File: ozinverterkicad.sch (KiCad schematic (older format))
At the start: 65 parts, among them P1 CONN_02X05, P2 CONN_01X02, P3 on/off, P4 temp, P5 ct sense, P6 Active mains, P7 neutral mains, P8 systemled, Q2 tip35c, T1 12vac transforme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

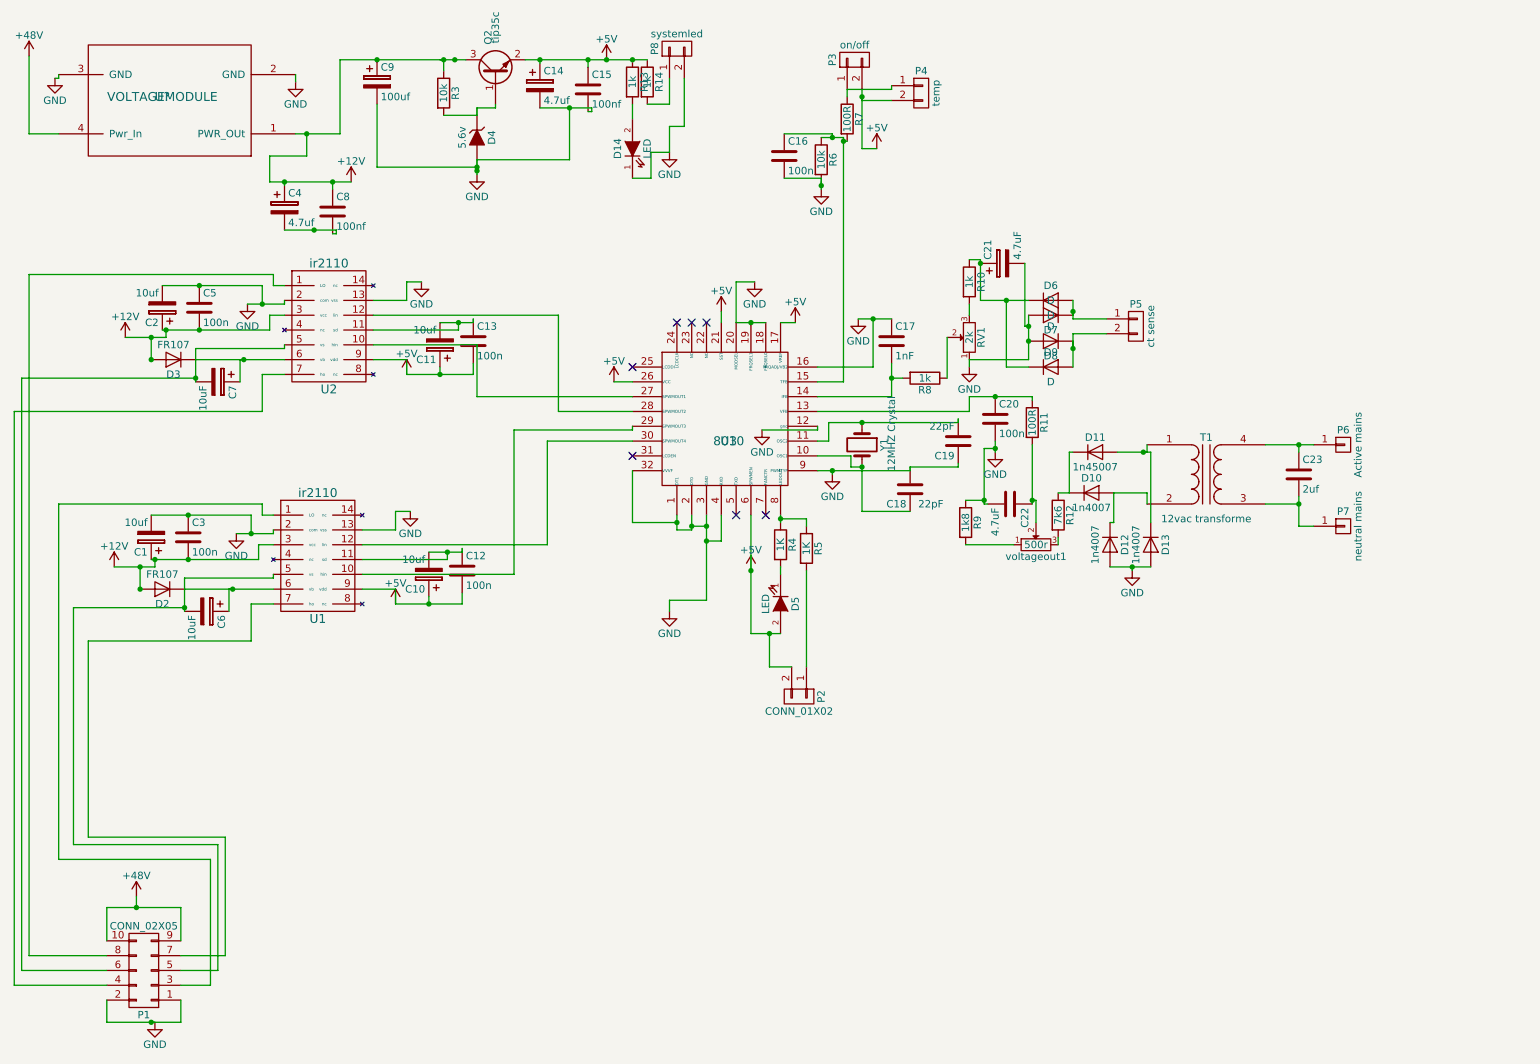
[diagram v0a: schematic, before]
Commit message: added extra ct sense
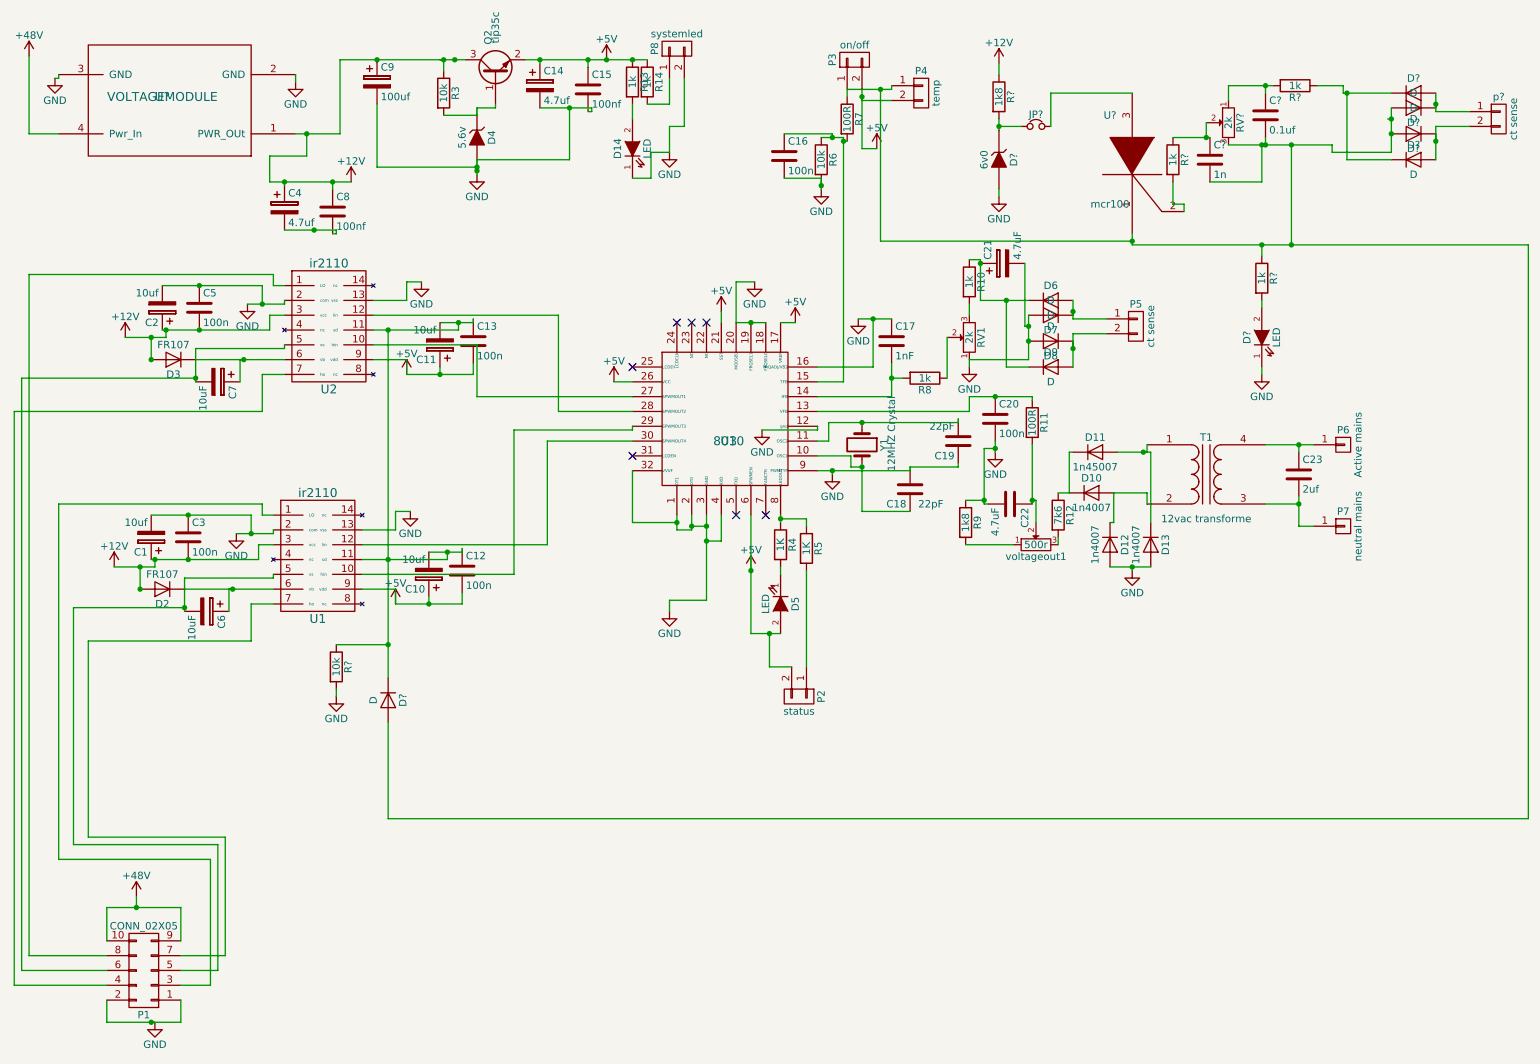
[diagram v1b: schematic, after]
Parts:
- added C?: 1n, symbol C
- added C?: 0.1uf, symbol C
- added D?: 6v0, symbol ZENER
- added D? (x4): D, Diodes_ThroughHole:Diode_DO-41_SOD81_Vertical_AnodeUp, symbol D
- added D?: LED, symbol LED
- added D?: D, symbol D
- added JP?: reset, symbol Jumper_NC_Small
- added R?: 1k8, symbol R
- added R? (x3): 1k, symbol R
- added R?: 10k, symbol R
- added RV?: 2k, Discret:RV2X4, symbol POT
- added U?: mcr100, symbol SCR
- added p?: ct sense, Connectors_Molex:Molex_KK-6410-02_02x2.54mm_Straight, symbol CONN_01X02
- P2: value CONN_01X02 -> status
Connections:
- net +12V: now also R?.1
- net GND: now also D?.1 (K), D?.2 (A), R?.2
- net at P3.1 (P1), P4.1 (P1), R7.1: now also C?.2, C?.2, D?.2 (A), D?.2 (A), D?.2 (A), R?.1, RV?.3, U?.1 (K)
- net at C11.2, C13.1, U2.11 (sd): now also C10.2, C12.1, U1.11 (sd), D?.1 (K), R?.1
- new net: D?.1 (K), JP?.1, R?.2
- new net: JP?.2, U?.3 (A)
- new net: D?.1 (K), D?.1 (K), R?.1
- new net: D?.1 (K), D?.2 (A), p?.1 (P1)
- new net: D?.1 (K), D?.2 (A), p?.2 (P2)
- new net: C?.1, R?.2, RV?.1
- new net: C?.1, R?.1, RV?.2
- new net: R?.2, U?.2 (G)
- new net: D?.2 (A), R?.2

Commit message: added extra ct routed
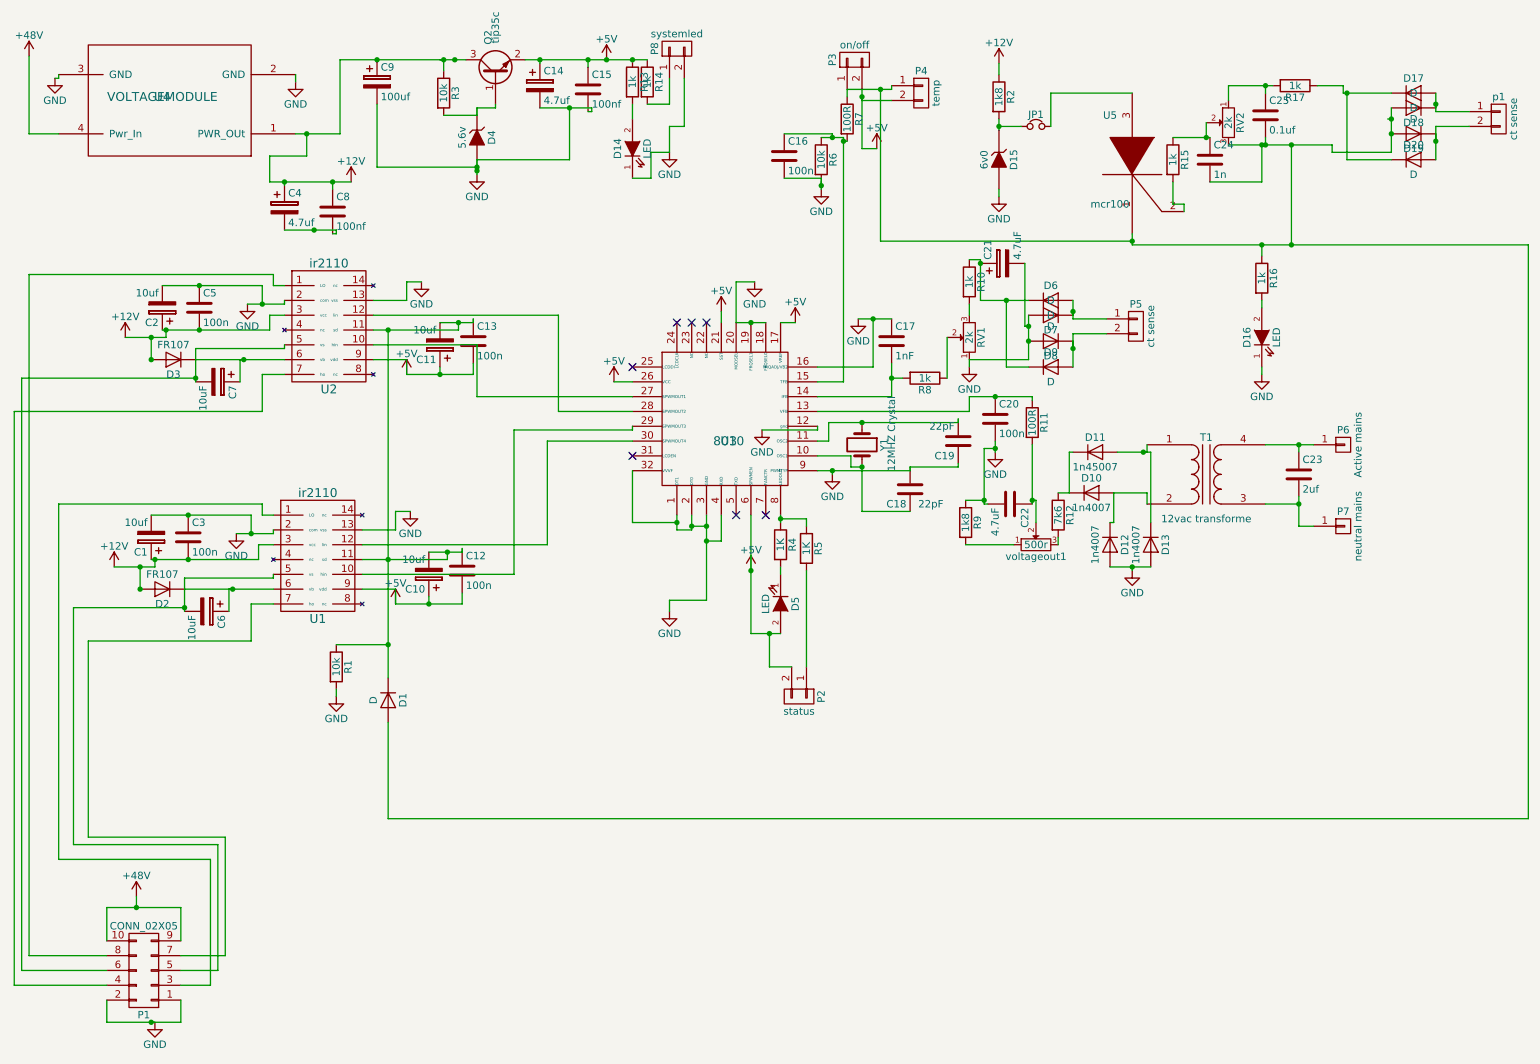
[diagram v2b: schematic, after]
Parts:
- C24: renamed from C?; footprint (none) -> Capacitors_ThroughHole:C_Disc_D3_P2.5
- C25: renamed from C?; footprint (none) -> Capacitors_ThroughHole:C_Radial_D5_L6_P2.5
- D1, D15: renamed from D?; footprint (none) -> Diodes_ThroughHole:Diode_DO-41_SOD81_Vertical_AnodeUp
- D16: renamed from D?; footprint (none) -> LEDs:LED-5MM
- JP1: renamed from JP?; footprint (none) -> Connectors_Molex:Molex_KK-6410-02_02x2.54mm_Straight
- R1, R15, R16, R17, R2: renamed from R?; footprint (none) -> Resistors_ThroughHole:Resistor_Horizontal_RM7mm
- U4: renamed from U?; footprint (none) -> ozinverterkicad:lm2596hvsmodule
- U5: renamed from U?; footprint (none) -> TO_SOT_Packages_THT:TO-92_Molded_Narrow
- gave numbers to parts that had none: 6
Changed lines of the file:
@@
 $EndComp
 $Comp
-L +12V #PWR027
+L +12V #PWR026
 U 1 1 57CBBFC9
 P 2825 1725
-F 0 "#PWR027" H 2825 1575 50  0001 C CNN
+F 0 "#PWR026" H 2825 1575 50  0001 C CNN
 F 1 "+12V" H 2825 1865 50  0000 C CNN
 F 2 "" H 2825 1725 50  0000 C CNN
@@
 $EndComp
 $Comp
-L GND #PWR028
+L GND #PWR027
 U 1 1 57CBD12F
 P 3675 1675
-F 0 "#PWR028" H 3675 1425 50  0001 C CNN
+F 0 "#PWR027" H 3675 1425 50  0001 C CNN
 F 1 "GND" H 3675 1525 50  0000 C CNN
 F 2 "" H 3675 1675 50  0000 C CNN
@@
 $EndComp
 $Comp
-L +5V #PWR029
+L +5V #PWR028
 U 1 1 57CBD147
 P 4550 900
-F 0 "#PWR029" H 4550 750 50  0001 C CNN
+F 0 "#PWR028" H 4550 750 50  0001 C CNN
 F 1 "+5V" H 4550 1040 50  0000 C CNN
 F 2 "" H 4550 900 50  0000 C CNN
@@
 $EndComp
 $Comp
-L GND #PWR030
+L GND #PWR029
 U 1 1 57CC63F3
 P 4975 1525
-F 0 "#PWR030" H 4975 1275 50  0001 C CNN
+F 0 "#PWR029" H 4975 1275 50  0001 C CNN
 F 1 "GND" H 4975 1375 50  0000 C CNN
 F 2 "" H 4975 1525 50  0000 C CNN
@@
 $EndComp
 $Comp
-L VOLTAGEMODULE U?
+L VOLTAGEMODULE U4
 U 1 1 57CBBBB1
 P 1550 1150
-F 0 "U?" H 1550 1150 60  0000 C CNN
+F 0 "U4" H 1550 1150 60  0000 C CNN
 F 1 "VOLTAGEMODULE" H 1550 1150 60  0000 C CNN
-F 2 "" H 1550 1150 60  0000 C CNN
+F 2 "ozinverterkicad:lm2596hvsmodule" H 1550 1150 60  0001 C CNN
 F 3 "" H 1550 1150 60  0000 C CNN
 	1    1550 1150
@@
 $EndComp
 $Comp
-L GND #PWR?
+L GND #PWR030
 U 1 1 57CBDA8B
 P 825 1025
-F 0 "#PWR?" H 825 775 50  0001 C CNN
+F 0 "#PWR030" H 825 775 50  0001 C CNN
 F 1 "GND" H 825 875 50  0000 C CNN
 F 2 "" H 825 1025 50  0000 C CNN
@@
 $EndComp
 $Comp
-L GND #PWR?
+L GND #PWR031
 U 1 1 57CBE302
 P 2450 1050
-F 0 "#PWR?" H 2450 800 50  0001 C CNN
+F 0 "#PWR031" H 2450 800 50  0001 C CNN
 F 1 "GND" H 2450 900 50  0000 C CNN
 F 2 "" H 2450 1050 50  0000 C CNN
@@
 $EndComp
 $Comp
-L ZENER D?
+L ZENER D15
 U 1 1 58022F88
 P 7200 1575
-F 0 "D?" H 7200 1675 50  0000 C CNN
+F 0 "D15" H 7200 1675 50  0000 C CNN
 F 1 "6v0" H 7200 1475 50  0000 C CNN
-F 2 "" H 7200 1575 50  0000 C CNN
+F 2 "Diodes_ThroughHole:Diode_DO-41_SOD81_Vertical_AnodeUp" H 7200 1575 50  0001 C CNN
 F 3 "" H 7200 1575 50  0000 C CNN
 	1    7200 1575
@@
 $EndComp
 $Comp
-L GND #PWR?
+L GND #PWR032
 U 1 1 580231C8
 P 7200 1825
-F 0 "#PWR?" H 7200 1575 50  0001 C CNN
+F 0 "#PWR032" H 7200 1575 50  0001 C CNN
 F 1 "GND" H 7200 1675 50  0000 C CNN
 F 2 "" H 7200 1825 50  0000 C CNN
@@
 $EndComp
 $Comp
-L R R?
+L R R2
 U 1 1 58023326
 P 7200 1150
-F 0 "R?" V 7280 1150 50  0000 C CNN
+F 0 "R2" V 7280 1150 50  0000 C CNN
 F 1 "1k8" V 7200 1150 50  0000 C CNN
-F 2 "" V 7130 1150 50  0000 C CNN
+F 2 "Resistors_ThroughHole:Resistor_Horizontal_RM7mm" V 7130 1150 50  0001 C CNN
 F 3 "" H 7200 1150 50  0000 C CNN
 	1    7200 1150
@@
 $EndComp
 $Comp
-L +12V #PWR?
+L +12V #PWR033
 U 1 1 580236D3
 P 7200 925
-F 0 "#PWR?" H 7200 775 50  0001 C CNN
+F 0 "#PWR033" H 7200 775 50  0001 C CNN
 F 1 "+12V" H 7200 1065 50  0000 C CNN
 F 2 "" H 7200 925 50  0000 C CNN
@@
 $EndComp
 $Comp
-L Jumper_NC_Small JP?
+L Jumper_NC_Small JP1
 U 1 1 58023CAC
 P 7450 1350
-F 0 "JP?" H 7450 1430 50  0000 C CNN
+F 0 "JP1" H 7450 1430 50  0000 C CNN
 F 1 "reset" H 7460 1290 50  0001 C CNN
-F 2 "" H 7450 1350 50  0000 C CNN
+F 2 "Connectors_Molex:Molex_KK-6410-02_02x2.54mm_Straight" H 7450 1350 50  0001 C CNN
 F 3 "" H 7450 1350 50  0000 C CNN
 	1    7450 1350
@@
 Connection ~ 7200 1350
 $Comp
-L D D?
+L D D17
 U 1 1 580262A2
 P 10000 1125
-F 0 "D?" H 10000 1225 50  0000 C CNN
+F 0 "D17" H 10000 1225 50  0000 C CNN
 F 1 "D" H 10000 1025 50  0000 C CNN
 F 2 "Diodes_ThroughHole:Diode_DO-41_SOD81_Vertical_AnodeUp" H 10000 1125 50  0001 C CNN
@@
 $EndComp
 $Comp
-L D D?
+L D D18
 U 1 1 580262A8
 P 10000 1225
-F 0 "D?" H 10000 1325 50  0000 C CNN
+F 0 "D18" H 10000 1325 50  0000 C CNN
 F 1 "D" H 10000 1125 50  0000 C CNN
 F 2 "Diodes_ThroughHole:Diode_DO-41_SOD81_Vertical_AnodeUp" H 10000 1225 50  0001 C CNN
@@
 $EndComp
 $Comp
-L D D?
+L D D19
 U 1 1 580262AE
 P 10000 1400
-F 0 "D?" H 10000 1500 50  0000 C CNN
+F 0 "D19" H 10000 1500 50  0000 C CNN
 F 1 "D" H 10000 1300 50  0000 C CNN
 F 2 "Diodes_ThroughHole:Diode_DO-41_SOD81_Vertical_AnodeUp" H 10000 1400 50  0001 C CNN
@@
 $EndComp
 $Comp
-L D D?
+L D D20
 U 1 1 580262B4
 P 10000 1575
-F 0 "D?" H 10000 1675 50  0000 C CNN
+F 0 "D20" H 10000 1675 50  0000 C CNN
 F 1 "D" H 10000 1475 50  0000 C CNN
 F 2 "Diodes_ThroughHole:Diode_DO-41_SOD81_Vertical_AnodeUp" H 10000 1575 50  0001 C CNN
@@
 $EndComp
 $Comp
-L CONN_01X02 p?
+L CONN_01X02 p1
 U 1 1 580262BA
 P 10575 1300
-F 0 "p?" H 10575 1450 50  0000 C CNN
+F 0 "p1" H 10575 1450 50  0000 C CNN
 F 1 "ct sense" V 10675 1300 50  0000 C CNN
 F 2 "Connectors_Molex:Molex_KK-6410-02_02x2.54mm_Straight" H 10575 1300 50  0001 C CNN
@@
 Connection ~ 9550 1125
 $Comp
-L R R?
+L R R17
 U 1 1 580267A1
 P 9200 1075
-F 0 "R?" V 9280 1075 50  0000 C CNN
+F 0 "R17" V 9280 1075 50  0000 C CNN
 F 1 "1k" V 9200 1075 50  0000 C CNN
-F 2 "" V 9130 1075 50  0000 C CNN
+F 2 "Resistors_ThroughHole:Resistor_Horizontal_RM7mm" V 9130 1075 50  0001 C CNN
 F 3 "" H 9200 1075 50  0000 C CNN
 	1    9200 1075
@@
 $EndComp
 $Comp
-L POT RV?
+L POT RV2
 U 1 1 58026D0E
 P 8750 1325
-F 0 "RV?" H 8750 1245 50  0000 C CNN
+F 0 "RV2" H 8750 1245 50  0000 C CNN
 F 1 "2k" H 8750 1325 50  0000 C CNN
 F 2 "Discret:RV2X4" H 8750 1325 50  0001 C CNN
@@
 	9450 1475 9450 1525
 $Comp
-L SCR U?
+L SCR U5
 U 1 1 58027CD5
 P 8100 1525
-F 0 "U?" H 8250 1775 50  0000 C CNN
+F 0 "U5" H 8250 1775 50  0000 C CNN
 F 1 "mcr100" H 8250 1175 50  0000 C CNN
-F 2 "" H 8100 1525 50  0000 C CNN
+F 2 "TO_SOT_Packages_THT:TO-92_Molded_Narrow" H 8100 1525 50  0001 C CNN
 F 3 "" H 8100 1525 50  0000 C CNN
 	1    8100 1525
@@
 	7550 1125 8100 1125
 $Comp
-L R R?
+L R R15
 U 1 1 58028060
 P 8375 1575
-F 0 "R?" V 8455 1575 50  0000 C CNN
+F 0 "R15" V 8455 1575 50  0000 C CNN
 F 1 "1k" V 8375 1575 50  0000 C CNN
-F 2 "" V 8305 1575 50  0000 C CNN
+F 2 "Resistors_ThroughHole:Resistor_Horizontal_RM7mm" V 8305 1575 50  0001 C CNN
 F 3 "" H 8375 1575 50  0000 C CNN
 	1    8375 1575
@@
 $EndComp
 $Comp
-L C C?
+L C C24
 U 1 1 58028119
 P 8625 1575
-F 0 "C?" H 8650 1675 50  0000 L CNN
+F 0 "C24" H 8650 1675 50  0000 L CNN
 F 1 "1n" H 8650 1475 50  0000 L CNN
-F 2 "" H 8663 1425 50  0000 C CNN
+F 2 "Capacitors_ThroughHole:C_Disc_D3_P2.5" H 8663 1425 50  0001 C CNN
 F 3 "" H 8625 1575 50  0000 C CNN
 	1    8625 1575
@@
 	7200 1825 7200 1775
 $Comp
-L C C?
+L C C25
 U 1 1 580293AE
 P 9000 1275
-F 0 "C?" H 9025 1375 50  0000 L CNN
+F 0 "C25" H 9025 1375 50  0000 L CNN
 F 1 "0.1uf" H 9025 1175 50  0000 L CNN
-F 2 "" H 9038 1125 50  0000 C CNN
+F 2 "Capacitors_ThroughHole:C_Radial_D5_L6_P2.5" H 9038 1125 50  0001 C CNN
 F 3 "" H 9000 1275 50  0000 C CNN
 	1    9000 1275
@@
 Connection ~ 9000 1475
 $Comp
-L R R?
+L R R16
 U 1 1 5802A0D3
 P 8975 2375
-F 0 "R?" V 9055 2375 50  0000 C CNN
+F 0 "R16" V 9055 2375 50  0000 C CNN
 F 1 "1k" V 8975 2375 50  0000 C CNN
-F 2 "" V 8905 2375 50  0000 C CNN
+F 2 "Resistors_ThroughHole:Resistor_Horizontal_RM7mm" V 8905 2375 50  0001 C CNN
 F 3 "" H 8975 2375 50  0000 C CNN
 	1    8975 2375
@@
 $EndComp
 $Comp
-L LED D?
+L LED D16
 U 1 1 5802A3B1
 P 8975 2775
-F 0 "D?" H 8975 2875 50  0000 C CNN
+F 0 "D16" H 8975 2875 50  0000 C CNN
 F 1 "LED" H 8975 2675 50  0000 C CNN
-F 2 "" H 8975 2775 50  0000 C CNN
+F 2 "LEDs:LED-5MM" H 8975 2775 50  0001 C CNN
 F 3 "" H 8975 2775 50  0000 C CNN
 	1    8975 2775
@@
 Connection ~ 8975 2150
 $Comp
-L GND #PWR?
+L GND #PWR034
 U 1 1 5802A9C2
 P 8975 3025
-F 0 "#PWR?" H 8975 2775 50  0001 C CNN
+F 0 "#PWR034" H 8975 2775 50  0001 C CNN
 F 1 "GND" H 8975 2875 50  0000 C CNN
 F 2 "" H 8975 3025 50  0000 C CNN
@@
 Connection ~ 9175 2150
 $Comp
-L D D?
+L D D1
 U 1 1 5802B7A7
 P 3075 5225
-F 0 "D?" H 3075 5325 50  0000 C CNN
+F 0 "D1" H 3075 5325 50  0000 C CNN
 F 1 "D" H 3075 5125 50  0000 C CNN
-F 2 "" H 3075 5225 50  0000 C CNN
+F 2 "Diodes_ThroughHole:Diode_DO-41_SOD81_Vertical_AnodeUp" H 3075 5225 50  0001 C CNN
 F 3 "" H 3075 5225 50  0000 C CNN
 	1    3075 5225
@@
 Connection ~ 3075 2725
 $Comp
-L R R?
+L R R1
 U 1 1 5802D08C
 P 2725 5000
-F 0 "R?" V 2805 5000 50  0000 C CNN
+F 0 "R1" V 2805 5000 50  0000 C CNN
 F 1 "10k" V 2725 5000 50  0000 C CNN
-F 2 "" V 2655 5000 50  0000 C CNN
+F 2 "Resistors_ThroughHole:Resistor_Horizontal_RM7mm" V 2655 5000 50  0001 C CNN
 F 3 "" H 2725 5000 50  0000 C CNN
 	1    2725 5000
@@
 Connection ~ 3075 4850
 $Comp
-L GND #PWR?
+L GND #PWR035
 U 1 1 5802D4AA
 P 2725 5200
-F 0 "#PWR?" H 2725 4950 50  0001 C CNN
+F 0 "#PWR035" H 2725 4950 50  0001 C CNN
 F 1 "GND" H 2725 5050 50  0000 C CNN
 F 2 "" H 2725 5200 50  0000 C CNN
